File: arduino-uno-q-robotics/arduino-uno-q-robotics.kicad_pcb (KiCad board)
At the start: 4 copper layers, 68.6 x 53.3 mm, 15 parts, among them J1 Conn_02x30_Odd_Even, J2 Conn_02x30_Odd_Even, J3 Connector_FFC-FPC, J5 Conn_02x13_Odd_Even, J6 Conn_02x04_Odd_Even, U1 LSM6DSO32, U2 TCA9803

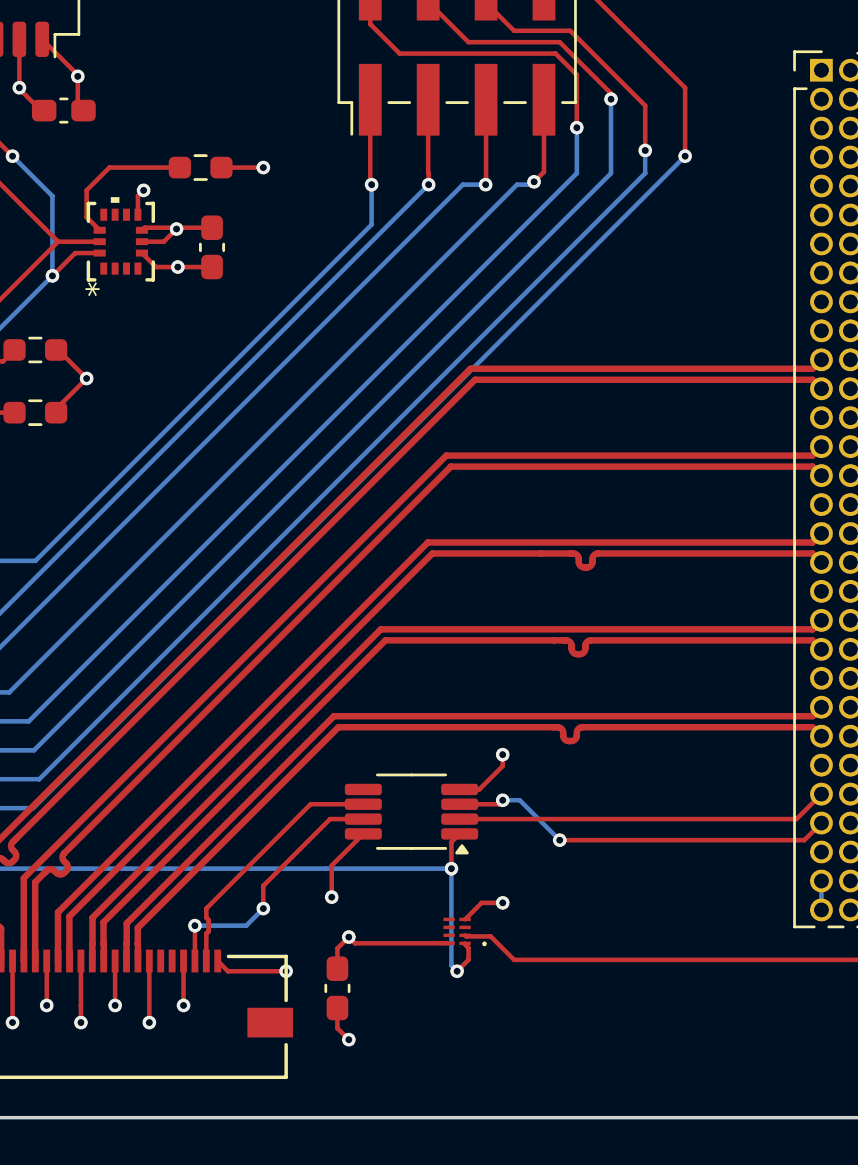
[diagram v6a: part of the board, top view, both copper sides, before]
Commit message: Adjust MCLK traces/vias
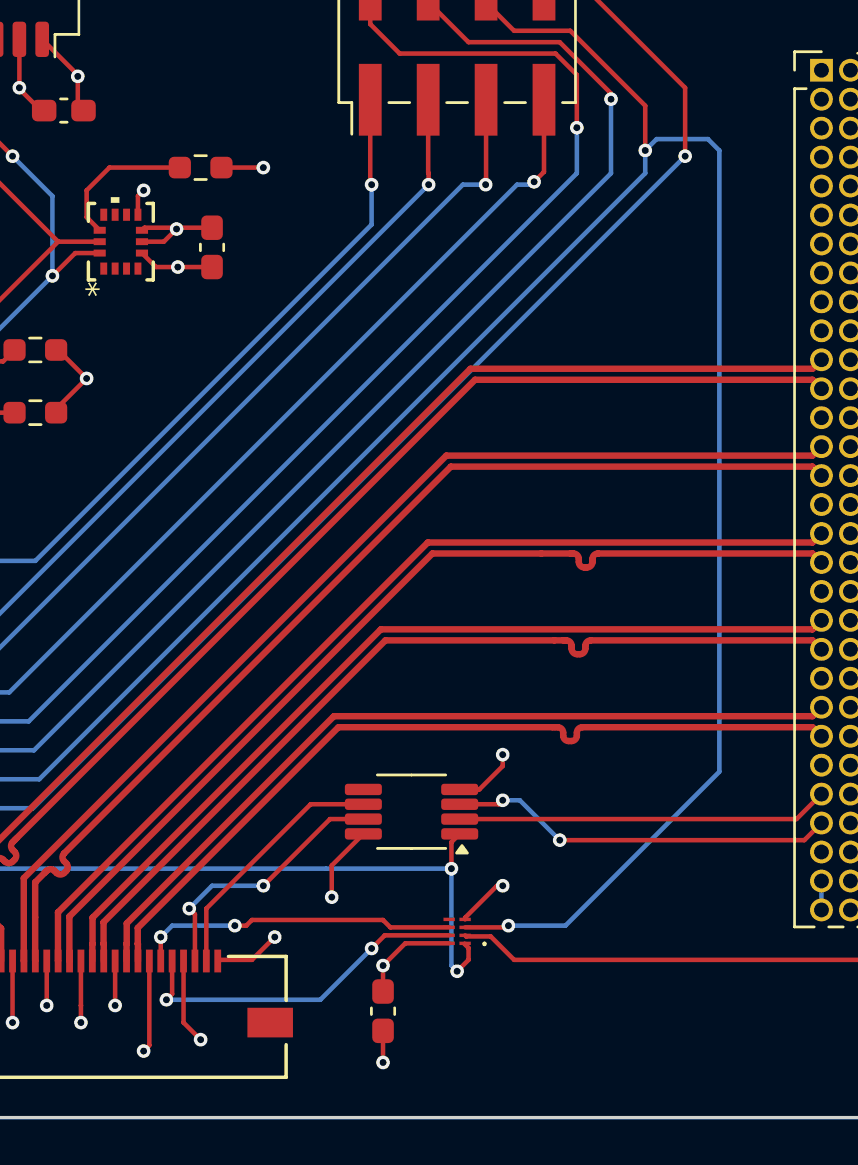
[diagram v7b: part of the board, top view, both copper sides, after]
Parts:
- moved C1 2.24 mm to (153.2, 116.2)
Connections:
- J3 pad 17: unconnected-(J3-Pad17) -> /SOC_GPIO_18_3.3V
- J3 pad 18: unconnected-(J3-Pad18) -> /SOC_CAM_MCLK0_3.3V
- U6 pad 3: unconnected-(U6-2A-Pad3) -> /SOC_GPIO_18
- U6 pad 6: unconnected-(U6-2B-Pad6) -> /SOC_GPIO_18_3.3V
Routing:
- net /SOC_GPIO_18: track 65.1 -> 110.0 mm, vias 1 -> 2
- net /SOC_CAM_MCLK0_3.3V: track 0.00 -> 15.4 mm, vias 0 -> 2
- net /SOC_GPIO_18_3.3V: track 0.00 -> 14.1 mm, vias 0 -> 2
- net GND: track 49.6 -> 52.9 mm
- net +3.3V: track 32.2 -> 30.3 mm

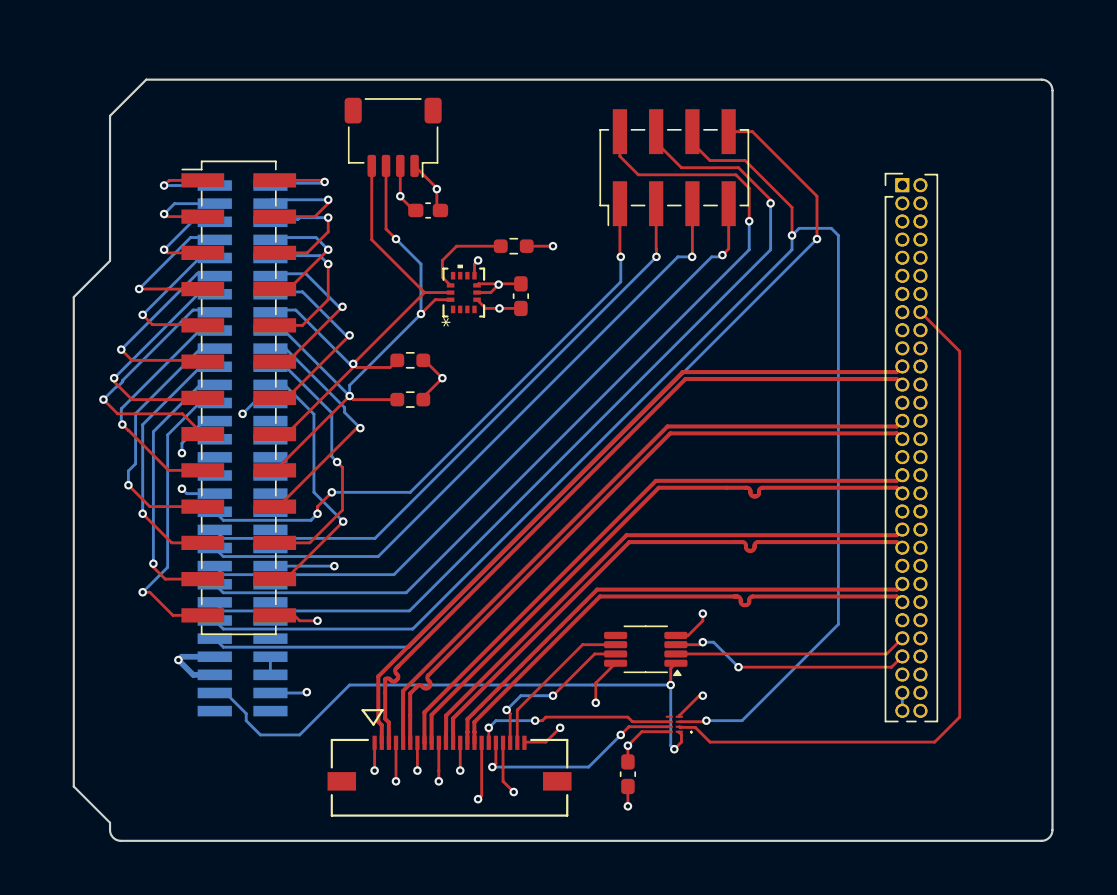
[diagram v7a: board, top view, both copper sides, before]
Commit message: Adjust ground pour for front and back layer
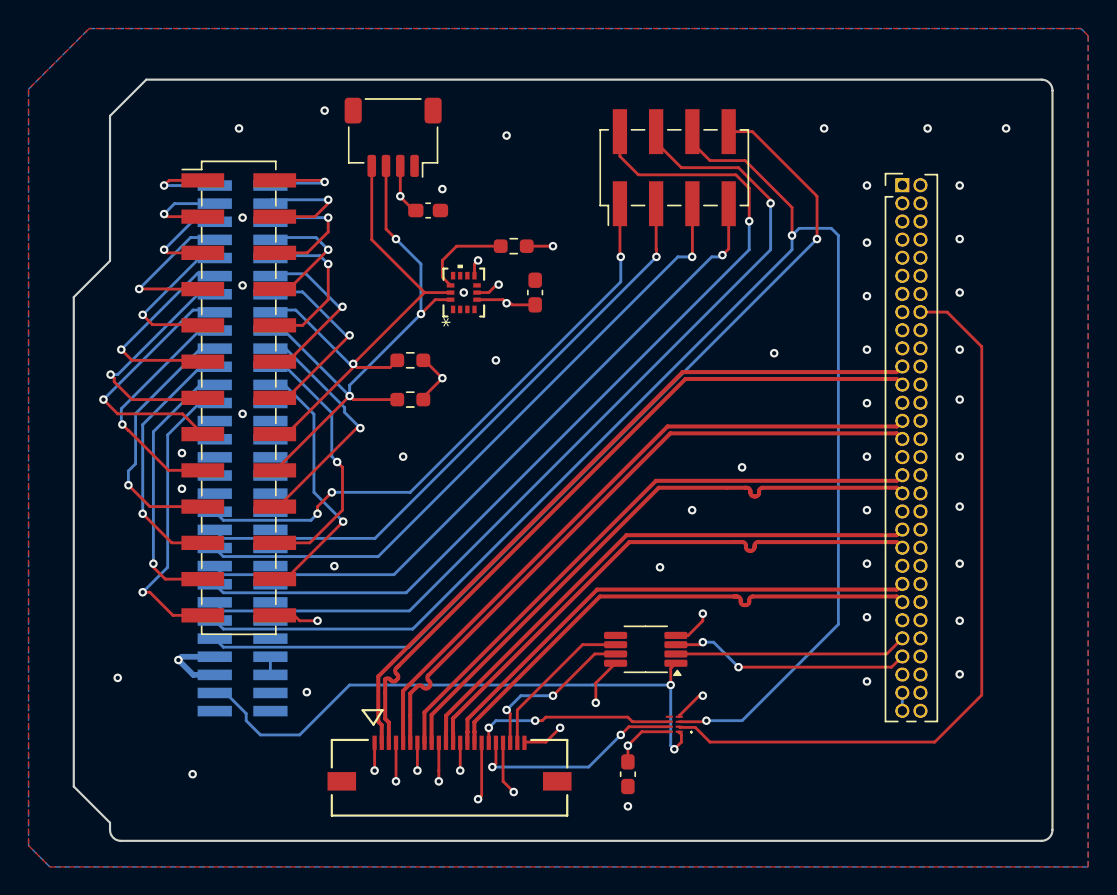
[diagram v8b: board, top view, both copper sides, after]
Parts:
- moved C4 1.03 mm to (146.8, 82.5)
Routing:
- net GND: track 52.9 -> 29.7 mm, vias 18 -> 55
- net /SOC_CAM_MCLK0: track 50.3 -> 52.7 mm
- net +3.3V: track 30.3 -> 31.4 mm
- added copper zone on B.Cu, net GND
- added copper zone on F.Cu, net GND
